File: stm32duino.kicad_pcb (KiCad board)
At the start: 2 copper layers, 87.6 x 48.3 mm, 20 parts, among them P1 CONN_02X07, P2 CONN_01X04, P3 DISP_SER, P4 HOST_SER, U1 stm32f103c8t6-module-china

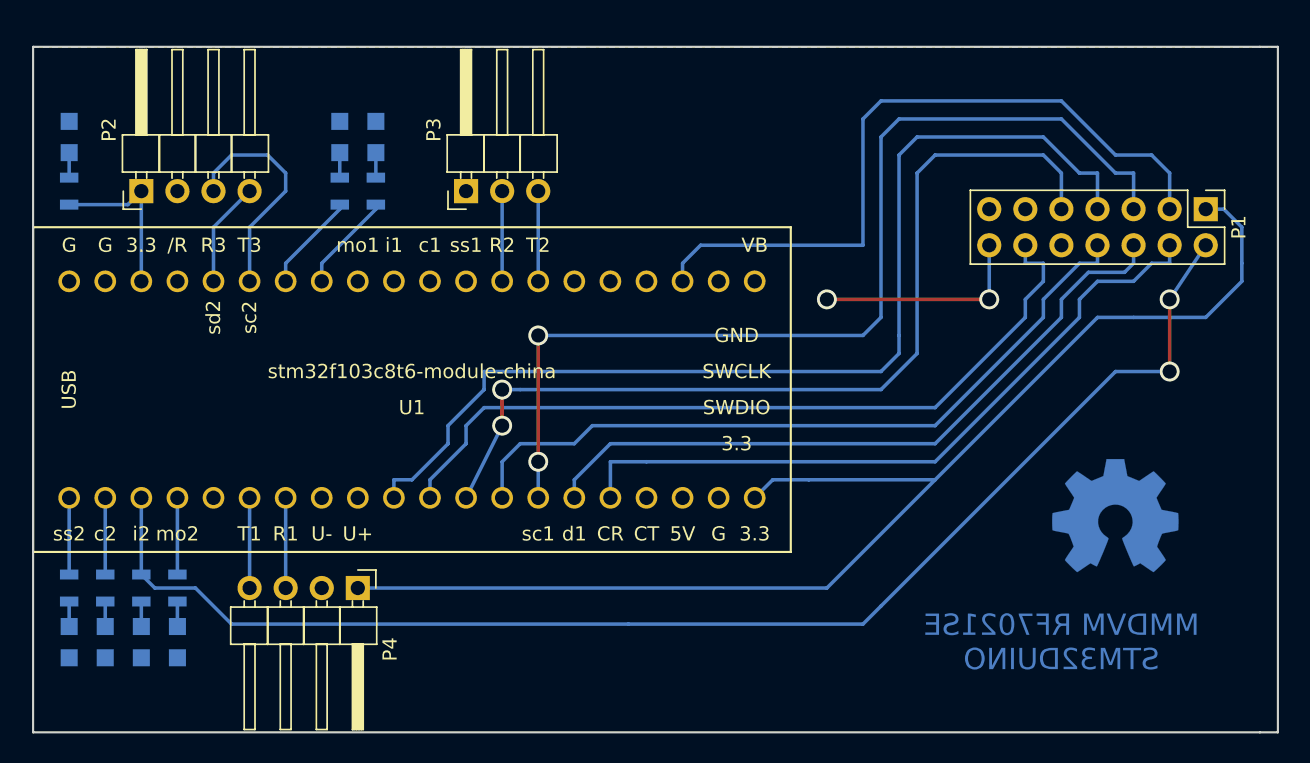
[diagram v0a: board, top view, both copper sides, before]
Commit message: Moved LEDs and other components around, added mounting holes.
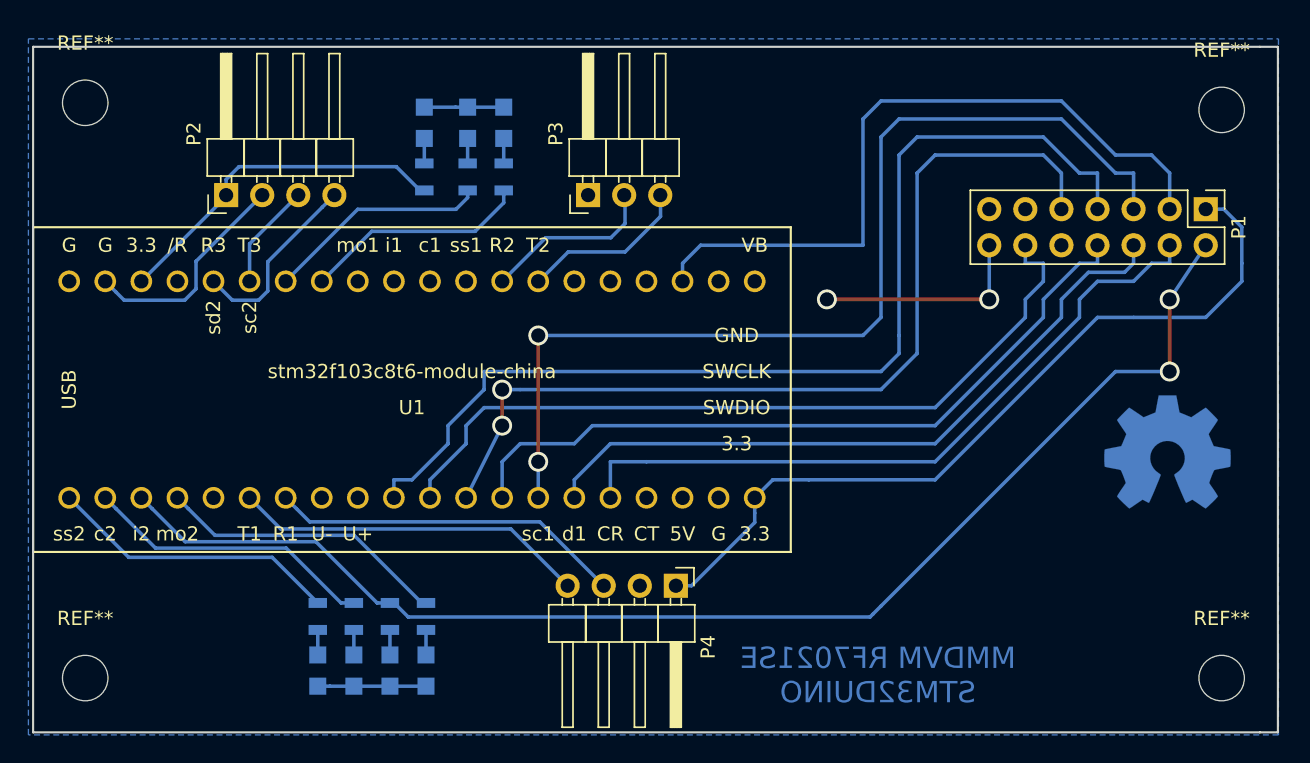
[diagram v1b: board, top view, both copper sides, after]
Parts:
- added REF**: MountingHole_3.2mm_M3, Mounting_Holes:MountingHole_3.2mm_M3, F.Cu at (104.0, 39.5)
- added REF**: MountingHole_3.2mm_M3, Mounting_Holes:MountingHole_3.2mm_M3, F.Cu at (104.0, 80.0)
- added REF**: MountingHole_3.2mm_M3, Mounting_Holes:MountingHole_3.2mm_M3, F.Cu at (184.0, 80.0)
- added REF**: MountingHole_3.2mm_M3, Mounting_Holes:MountingHole_3.2mm_M3, F.Cu at (184.0, 40.0)
- moved D7 25.0 mm to (127.9, 40.9)
- moved R7 25.0 mm to (127.9, 44.7)
- moved P4 22.4 mm to (145.6, 73.5)
- moved D1 17.6 mm to (122.9, 79.5)
- moved D3 17.6 mm to (120.4, 79.5)
- moved D4 17.6 mm to (125.5, 79.5)
- moved D5 17.6 mm to (128.0, 79.5)
- moved R1 17.6 mm to (122.9, 75.7)
- moved R3 17.6 mm to (120.4, 75.7)
- moved R4 17.6 mm to (125.5, 75.7)
- moved R5 17.6 mm to (128.0, 75.7)
- moved D6 9.06 mm to (133.5, 40.9)
- moved R6 9.06 mm to (133.5, 44.7)
- moved D2 9.06 mm to (130.9, 40.9)
- moved R2 9.06 mm to (130.9, 44.7)
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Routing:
- net GND: track 15.2 -> 44.3 mm
- net +3V3: track 103.1 -> 81.3 mm
- net HOST_TX: track 6.35 -> 25.0 mm
- net HOST_RX: track 6.35 -> 25.0 mm
- net LED_COS: track 5.40 -> 20.6 mm
- net LEDDMR: track 5.40 -> 20.6 mm
- net LEDDSTAR: track 5.40 -> 20.6 mm
- net LEDP25: track 6.98 -> 16.3 mm
- net LEDYSF: track 6.98 -> 16.1 mm
- net Net-(P2-Pad3): track 16.1 -> 7.49 mm
- net DISP_RX: track 6.35 -> 12.6 mm
- net Net-(P2-Pad4): track 7.40 -> 13.3 mm
- net DISP_TX: track 6.35 -> 12.0 mm
- net PAC: track 96.3 -> 92.7 mm

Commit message: Moved LEDs around, grouped them by logical function.
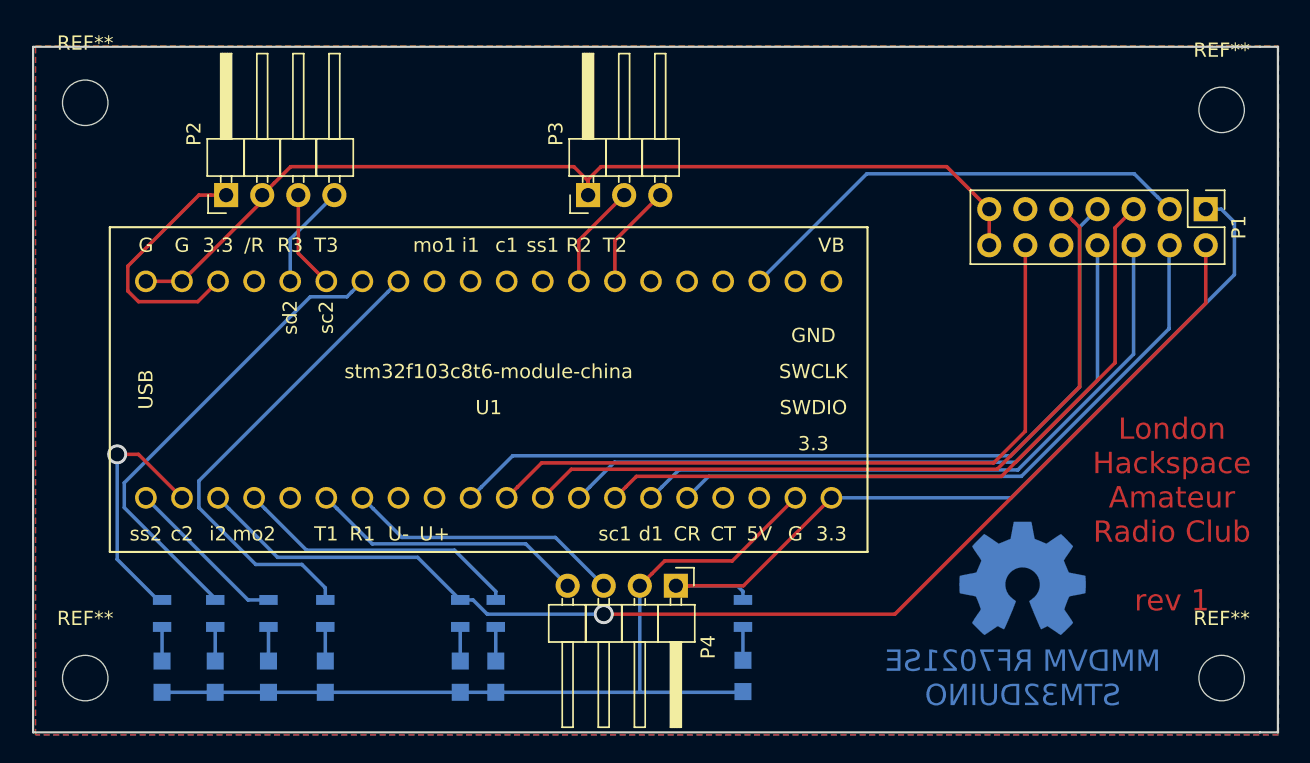
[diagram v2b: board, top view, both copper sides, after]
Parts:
- D1: value LED -> LED_DMR
- D2: value LED -> LED_YSF
- D3: value LED -> LED_DSTAR
- D4: value LED -> LED_PAC
- D5: value LED -> LED_COS
- D6: value LED -> LED_P25
- D7: value LED -> LED_33V
- P1: value CONN_02X07 -> RF7021SE
- P2: value CONN_01X04 -> DISP_I2C
- moved D7 44.9 mm to (150.3, 79.8), turned to 90 degrees
- moved D2 42.8 mm to (113.2, 79.9), turned to 90 degrees
- moved D6 41.0 mm to (120.9, 79.9), turned to 90 degrees
- moved R7 38.0 mm to (150.3, 75.5), turned to 270 degrees
- moved R2 35.5 mm to (113.2, 75.5), turned to 270 degrees
- moved R6 33.2 mm to (120.9, 75.5), turned to 270 degrees
- moved REF*** 13.5 mm to (170.0, 73.0)
- moved D1 13.5 mm to (109.4, 79.9)
- moved R1 13.5 mm to (109.4, 75.5)
- moved U1 5.40 mm to (132.4, 59.7)
- moved D4 4.97 mm to (130.4, 79.9)
- moved R4 4.95 mm to (130.4, 75.5)
- moved D5 4.93 mm to (132.9, 79.9)
- moved R5 4.91 mm to (132.9, 75.5)
- moved D3 3.50 mm to (116.9, 79.9)
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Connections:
- P1 pad 10: Net-(P1-Pad10) -> (no net)
- P1 pad 11: Net-(P1-Pad11) -> (no net)
- U1 pad 17: Net-(U1-Pad17) -> (no net)
- U1 pad 18: Net-(U1-Pad18) -> (no net)
- U1 pad 21: Net-(U1-Pad21) -> (no net)
- U1 pad 22: Net-(U1-Pad22) -> (no net)
- U1 pad 24: Net-(U1-Pad24) -> (no net)
- U1 pad 25: Net-(U1-Pad25) -> (no net)
- U1 pad 26: Net-(U1-Pad26) -> (no net)
- U1 pad 29: Net-(U1-Pad29) -> (no net)
- U1 pad 30: Net-(U1-Pad30) -> (no net)
- U1 pad 31: Net-(U1-Pad31) -> (no net)
- U1 pad 32: Net-(U1-Pad32) -> (no net)
- U1 pad 37: Net-(U1-Pad37) -> (no net)
- U1 pad 5: Net-(U1-Pad5) -> (no net)
- U1 pad 8: Net-(U1-Pad8) -> (no net)
- U1 pad 9: Net-(U1-Pad9) -> (no net)
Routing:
- net GND: track 44.3 -> 131.6 mm, vias 2 -> 0
- net SDATA: track 71.2 -> 50.5 mm, vias 2 -> 0
- net LEDP25: track 16.3 -> 33.8 mm
- net LEDYSF: track 16.1 -> 33.5 mm
- net CE: track 50.1 -> 33.1 mm
- net CLKOUT: track 74.1 -> 59.1 mm
- net DATAOUT: track 64.9 -> 54.1 mm, vias 2 -> 0
- net LEDDSTAR: track 20.6 -> 11.6 mm
- net PAC: track 92.7 -> 86.1 mm, vias 2 -> 1
- net Net-(P2-Pad4): track 13.3 -> 7.36 mm
- net HOST_TX: track 25.0 -> 19.6 mm
- net HOST_RX: track 25.0 -> 19.6 mm
- net DISP_RX: track 12.6 -> 7.39 mm
- net SLE: track 49.7 -> 44.7 mm
- net DISP_TX: track 12.0 -> 7.39 mm
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- added copper zone on F.Cu, net GND
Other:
- board text added: "London Hackspace Amateur Radio Club rev 1"
